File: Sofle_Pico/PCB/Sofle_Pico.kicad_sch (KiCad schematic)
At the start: 121 parts, among them J1 Conn_01x05, J2 MJ-4PP-9, J3 Conn_01x04, J4 Conn_01x04, J5 Conn_01x05, J6 Conn_01x05, J7 Conn_01x04, Q1 DMG2305UX, SW1 SW_PUSH, SW10 SW_PUSH, SW11 SW_PUSH, SW12 SW_PUSH, SW13 SW_PUSH, SW14 SW_PUSH, SW15 SW_PUSH, SW16 SW_PUSH, SW17 SW_PUSH, SW18 SW_PUSH, SW19 SW_PUSH, SW2 SW_PUSH, SW20 SW_PUSH, SW21 SW_PUSH, SW22 SW_PUSH, SW23 SW_PUSH, SW24 SW_PUSH, SW25 Rotary_Encoder_Switch-Device, SW26 SW_PUSH, SW27 SW_PUSH, SW28 SW_PUSH, SW29 SW_PUSH, SW3 SW_PUSH, SW30 SW_PUSH, SW4 SW_PUSH, SW5 SW_PUSH, SW6 SW_PUSH, SW7 SW_PUSH, SW8 SW_PUSH, SW9 SW_PUSH, U1 SN74AHCT1G125, U2 Pico

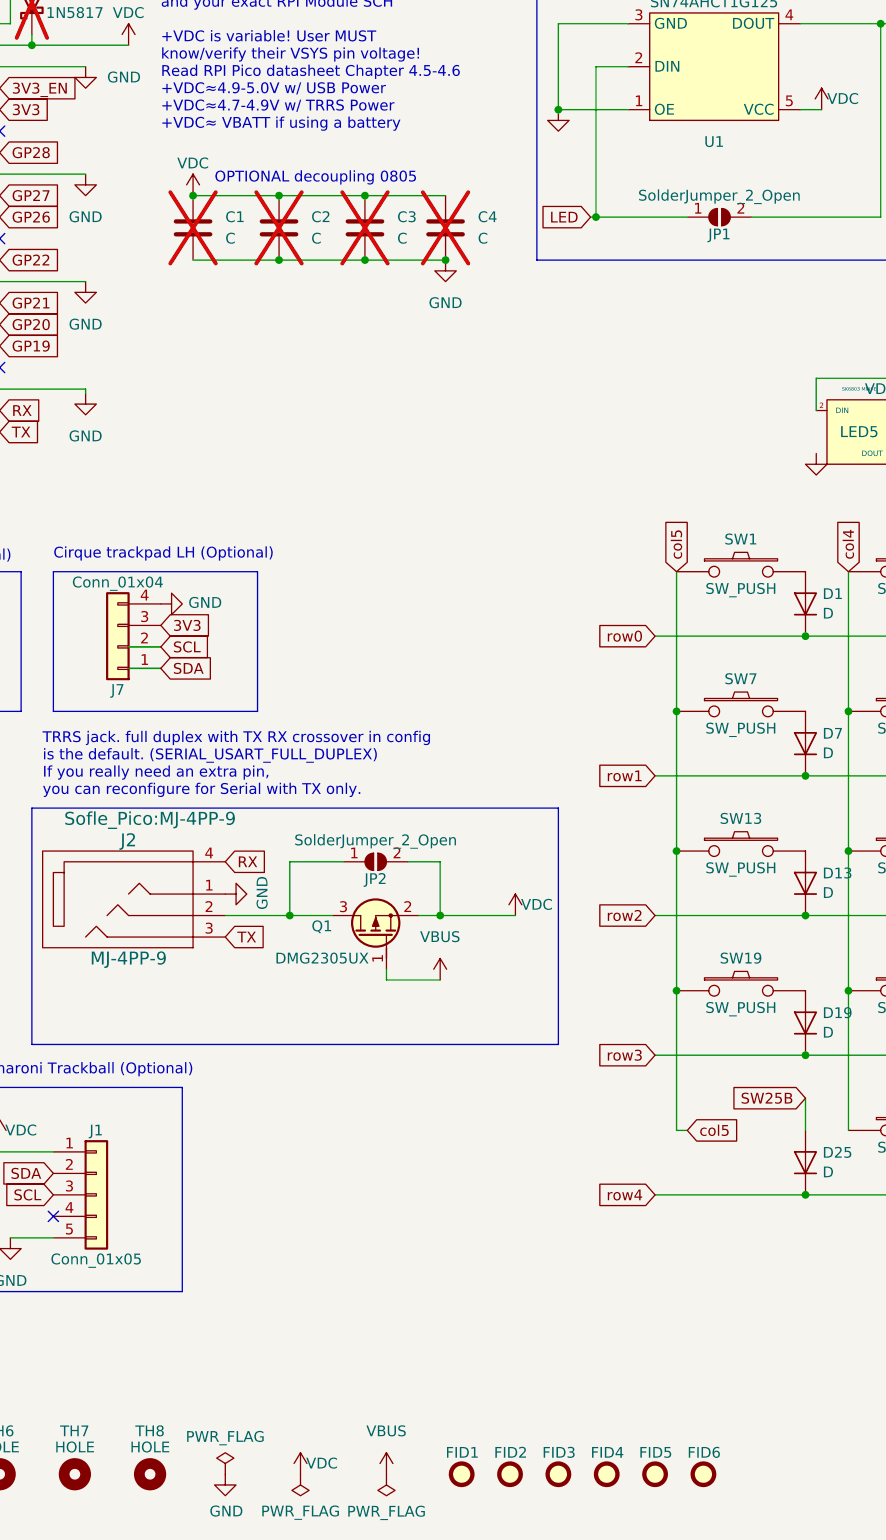
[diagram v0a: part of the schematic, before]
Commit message: Added soldermask pullbacks to board edges with manual lines on F./B.Mask layers
Started updating SCH to use JLCPCB standard stocked parts for PFET/diodes/caps (need to look for level shifter)

Added left/right hand outline for handedness quick reference

Updated Chico boards to have keyplate SVG lines for chocv1
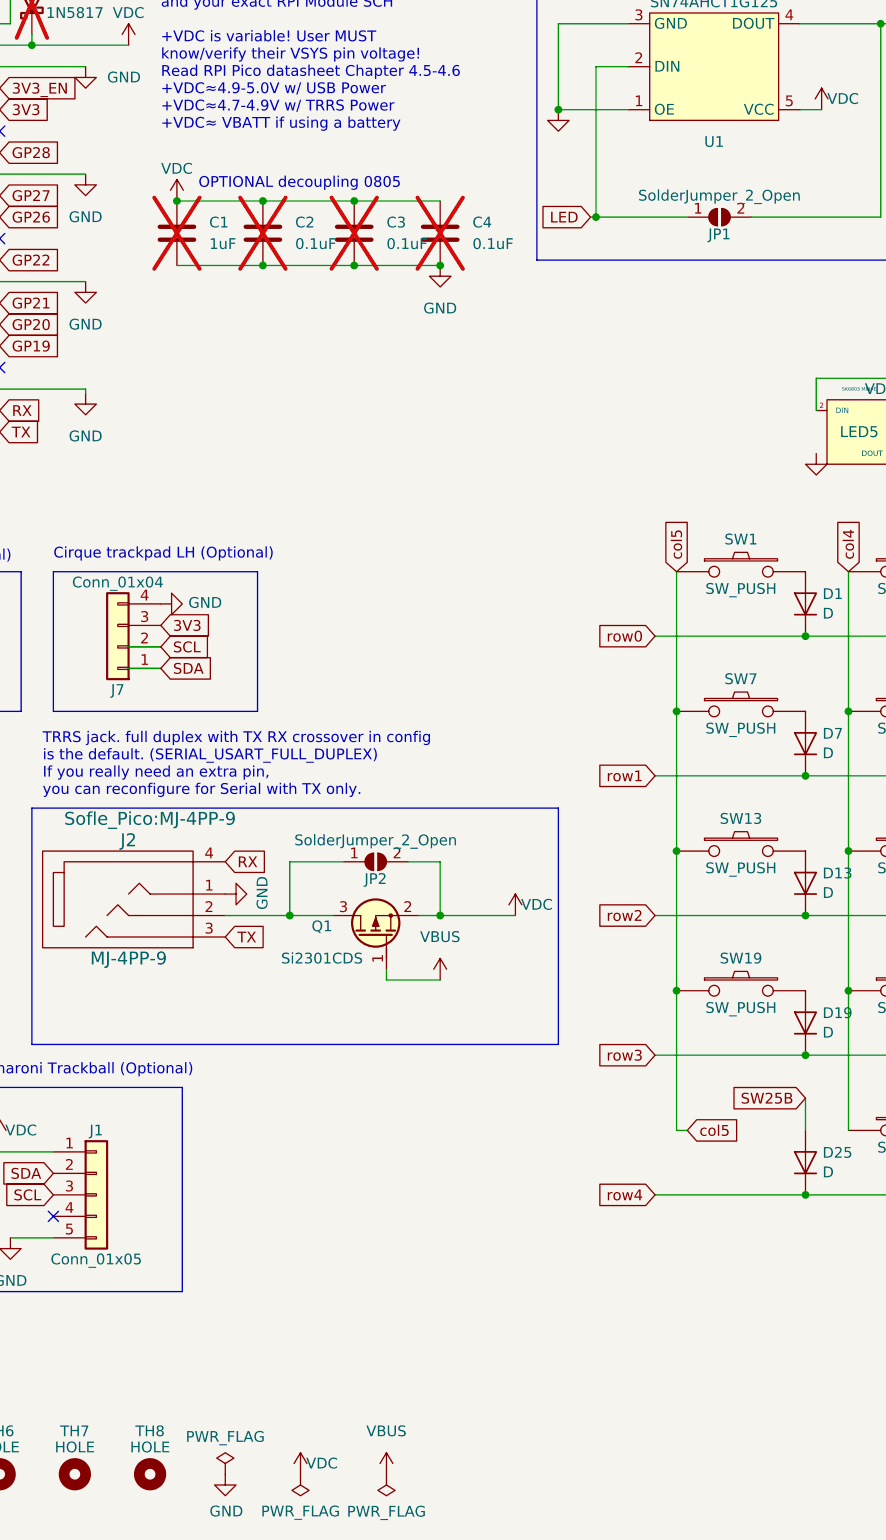
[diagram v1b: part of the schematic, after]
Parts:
- removed FID1, FID2, FID3, FID4, FID5, FID6: Fiducial, Fiducial:Fiducial_0.5mm_Mask1.5mm, symbol Mechanical:Fiducial
- C1: value C -> 1uF; Dielectric (none) -> X7R; MFG (none) -> Samsung; MFG PN (none) -> CL21B105KBFNNNE; Tolerance (%) (none) -> 10; Voltage Rating (none) -> 50V
- C2, C3, C4: value C -> 0.1uF; Dielectric (none) -> X7R; MFG (none) -> YAGEO; MFG PN (none) -> CC0805KRX7R9BB104; Tolerance (%) (none) -> 10; Voltage Rating (none) -> 50V
- D1, D10, D11, D12, D13, D14, D15, D16, D17, D18, D19, D2, D20, D21, D22, D23, D24, D25, D26, D27, D28, D29, D3, D30, D4, D5, D6, D7, D8, D9: MFG (none) -> Semtech; MFG PN (none) -> 1N4148W; Voltage Rating (none) -> 75v
- Q1: value DMG2305UX -> Si2301CDS; footprint Package_TO_SOT_SMD_AKL:SOT-23 -> Sofle_Pico:SOT-23_DS

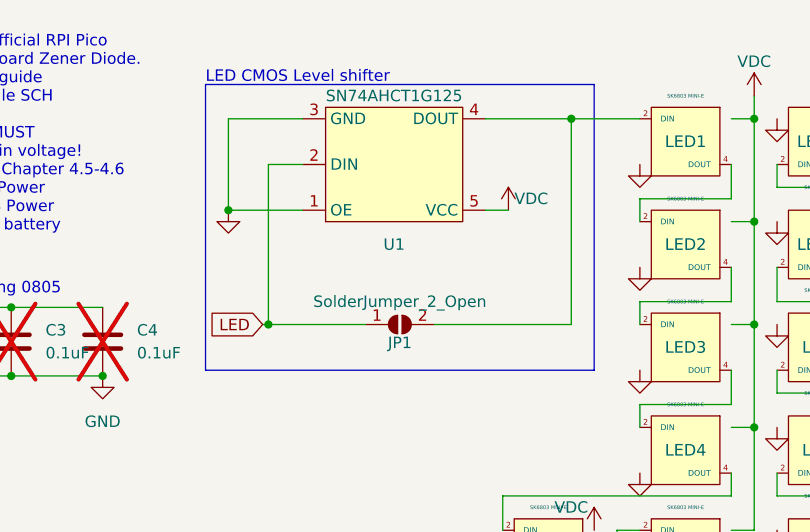
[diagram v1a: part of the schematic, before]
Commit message: Fixed overlapping holes in MX footprint that generated incorrect drill hit tables
Opened jumper soldermask apertures to allow for easier drag-solder bridging

Updated SCH to new buffer for JLCPCB "basic" part

Added JLCPCB PN params to parts for "basic" parts

Copied edge soldermask pullbacks from pico to chico
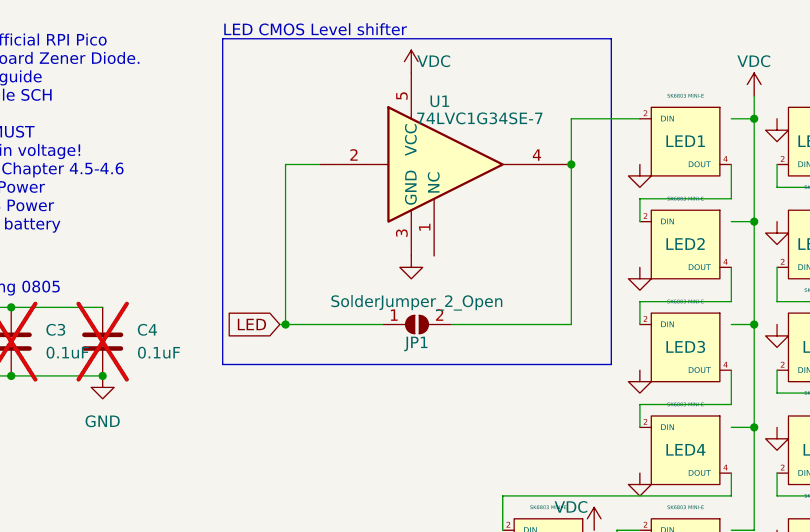
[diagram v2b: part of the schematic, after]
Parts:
- removed U1: SN74AHCT1G125, Junco:SN74AHCT1G125, symbol Sofle_Pico:SN74AHCT1G125
- added U1: 74LVC1G34SE-7, Package_TO_SOT_SMD:SOT-353_SC-70-5_Handsoldering, symbol 74xGxx:74LVC1G34
- C1: JLCPCB_PN# (none) -> C28323
- C2, C3, C4: JLCPCB_PN# (none) -> C49678
- D1, D10, D11, D12, D13, D14, D15, D16, D17, D18, D19, D2, D20, D21, D22, D23, D24, D25, D26, D27, D28, D29, D3, D30, D4, D5, D6, D7, D8, D9: JLCPCB_PN# (none) -> C81598
- Q1: JLCPCB_PN# (none) -> C10487
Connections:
- net GND: now also U1.3 (GND)
- net LED: now also U1.2
- net VDC: now also U1.5 (VCC)
- net at JP1.2 (B), LED1.2 (DIN): now also U1.4

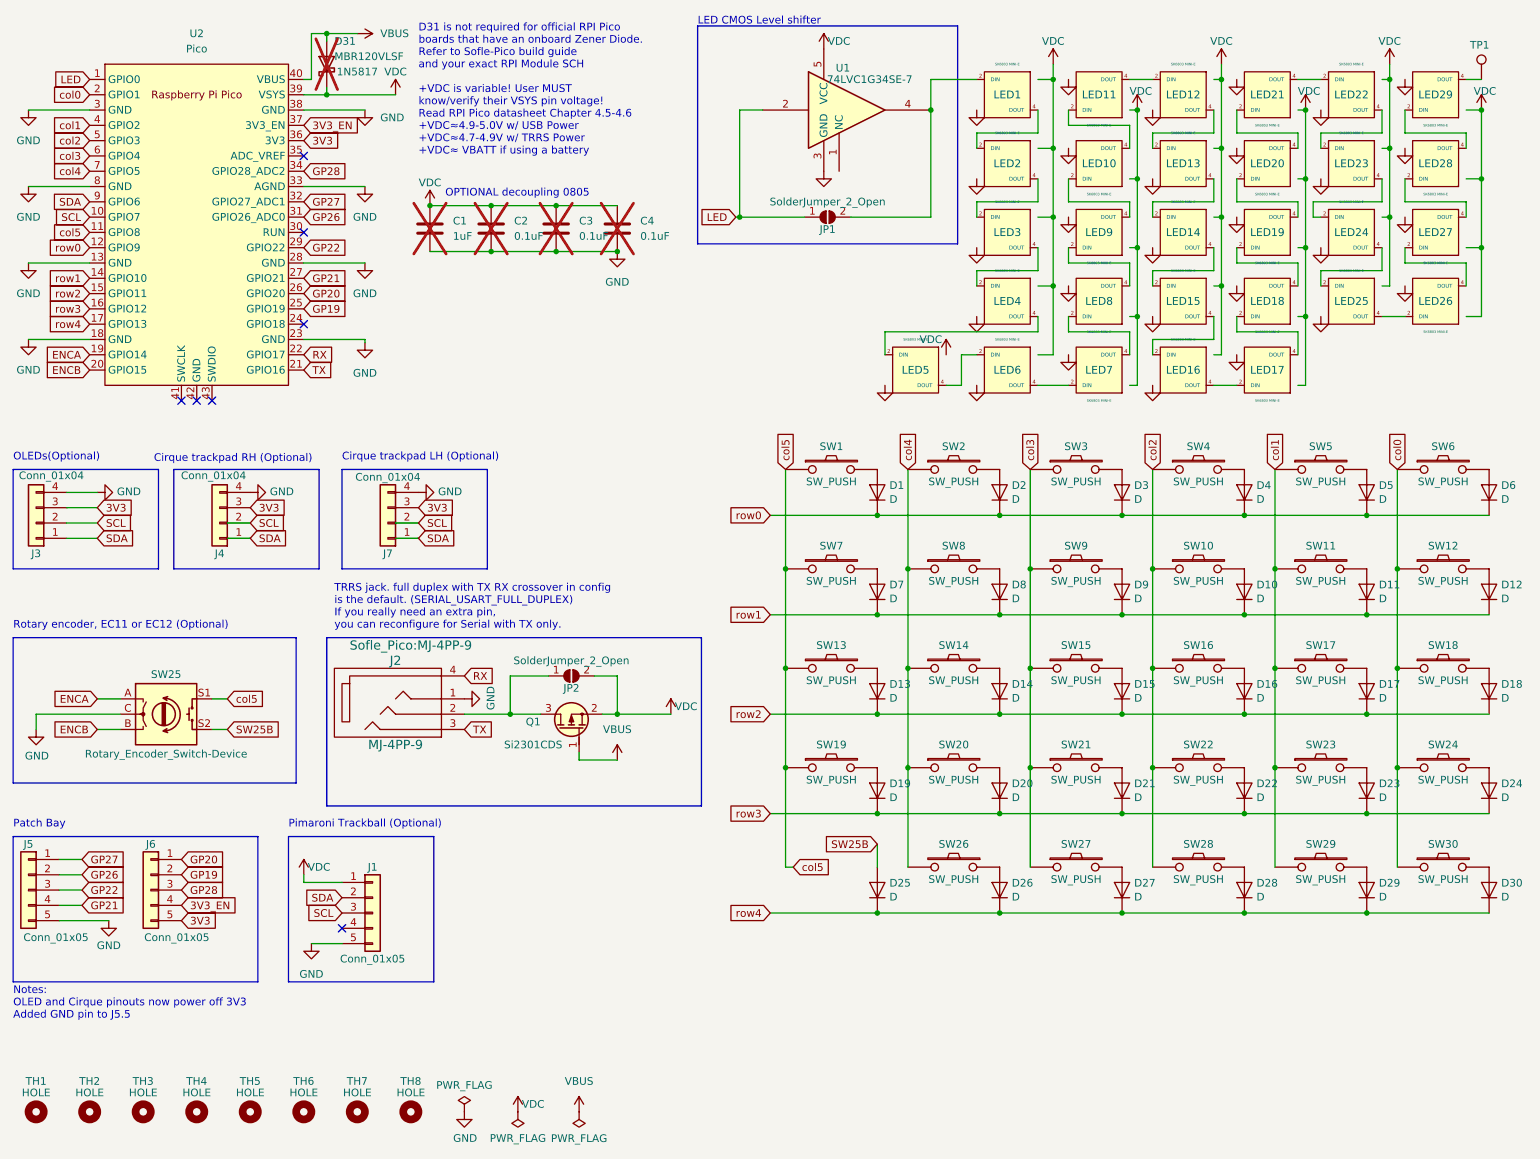
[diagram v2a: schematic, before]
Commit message: MX back conversion of Choc layout
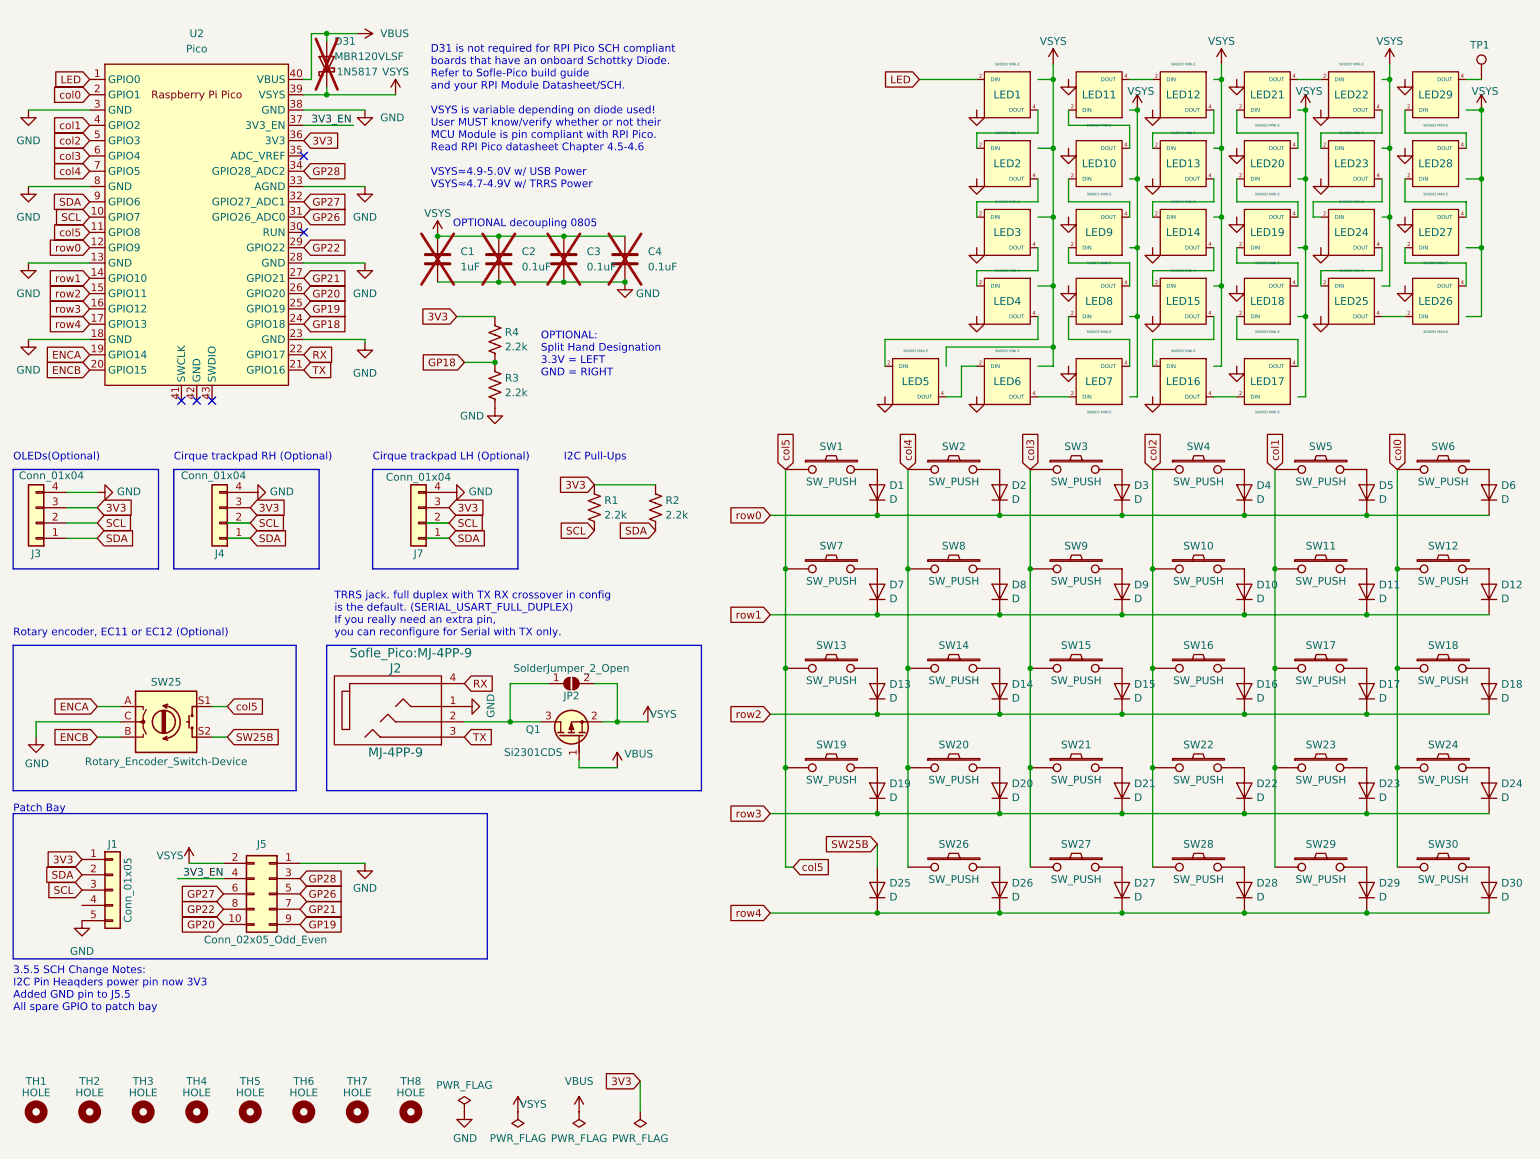
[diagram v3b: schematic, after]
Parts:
- removed J5, J6: Conn_01x05, Sofle_Pico:PinHeader_1x05_P2.54mm_Vertical, symbol Sofle_Pico:Conn_01x05
- removed JP1: SolderJumper_2_Open, Sofle_Pico:Level Shifter Bypass Jumper, symbol Sofle_Pico:SolderJumper_2_Open
- removed U1: 74LVC1G34SE-7, Package_TO_SOT_SMD:SOT-353_SC-70-5_Handsoldering, symbol 74xGxx:74LVC1G34
- added J5: Conn_02x05_Odd_Even, Connector_PinHeader_2.54mm:PinHeader_2x05_P2.54mm_Vertical, symbol Connector_Generic:Conn_02x05_Odd_Even
- added R1, R2, R3, R4: 2.2k, Sofle_Pico:Res_1206_SMD_6.3mm_TH_Hybrid, symbol Device:R_US
- C1: JLCPCB_PN (none) -> C28323; JLCPCB_PN# C28323 -> (none)
- C2, C3, C4: JLCPCB_PN (none) -> C49678; JLCPCB_PN# C49678 -> (none)
- D1, D10, D11, D12, D13, D14, D15, D16, D17, D18, D19, D2, D20, D21, D22, D23, D24, D25, D26, D27, D28, D29, D3, D30, D4, D5, D6, D7, D8, D9: JLCPCB_PN (none) -> C81598; JLCPCB_PN# C81598 -> (none)
- LED1, LED10, LED11, LED12, LED13, LED14, LED15, LED16, LED17, LED18, LED19, LED2, LED20, LED21, LED22, LED23, LED24, LED25, LED26, LED27, LED28, LED29, LED3, LED4, LED5, LED6, LED7, LED8, LED9: footprint Sofle_Pico:SK6803_MINI-E_V2 -> Sofle_Pico:SK6803_MINI-E_v3.5.5
- Q1: footprint Sofle_Pico:SOT-23_DS -> Package_TO_SOT_SMD_AKL:SOT-23; JLCPCB_PN (none) -> C10487; JLCPCB_PN# C10487 -> (none)
- SW1, SW10, SW11, SW12, SW13, SW14, SW15, SW16, SW17, SW18, SW19, SW2, SW20, SW21, SW22, SW23, SW24, SW26, SW27, SW28, SW29, SW3, SW30, SW4, SW5, SW6, SW7, SW8, SW9: footprint Sofle_Pico:Cherry_MX_DS_Hotswap_v3.5.4 -> Sofle_Pico:SW_MX_HS_DS_1u
- TH1, TH2, TH7: footprint Sofle_Pico:keyplate_hole_M2_standoff_passthrough -> Sofle_Pico:Hole from sofle for M2 posts gold rimmer wide-keyplate-hole
- TH3, TH4, TH6, TH8: footprint Sofle_Pico:keyplate_hole_M2_standoff_passthrough -> Sofle_Pico:Hole from sofle for M2 posts gold rimmer
- TH5: footprint (none) -> Sofle_Pico:Hole from sofle for M2 posts gold rimmer
- TP1: JLCPCB_PN (none) -> C94111
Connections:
- net 3V3: now also J1.1 (Pin_1), R1.1, R2.1, R4.2
- net 3V3_EN: now also J5.4 (Pin_4)
- net GND: now also J5.1 (Pin_1), R3.2
- net GP19: now also J5.9 (Pin_9)
- net GP20: now also J5.10 (Pin_10)
- net GP21: now also J5.7 (Pin_7)
- net GP22: now also J5.8 (Pin_8)
- net GP26: now also J5.5 (Pin_5)
- net GP27: now also J5.6 (Pin_6)
- net GP28: now also J5.3 (Pin_3)
- net LED: now also LED1.2 (DIN)
- net SCL: now also R1.2
- net SDA: now also R2.2
- net GP18: now reaches U2.24 (GPIO18)
- net GP18: now also R3.1, R4.1
- net VDC renamed VDD
- net VDD: now also J5.2 (Pin_2); no longer J1.1 (Pin_1)
- no-connect marks 7 -> 5
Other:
- note added: "3.5.5 SCH Change Notes: I2C Pin Heaqders power pin now 3V3 Added GND pin to J5.5 All spare GPIO to patch bay"
- note added: "D31 is not required for RPI Pico SCH compliant boards that have an onboard Schottky Diode. Refer to Sofle-Pico build guide and your RPI Module Datasheet/SCH. VSYS is variable depending on diode used! User MUST know/verify whether or not their MCU Module is pin compliant with RPI Pico. Read RPI Pico datasheet Chapter 4.5-4.6 VSYS≈4.9-5.0V w/ USB Power VSYS≈4.7-4.9V w/ TRRS Power"
- note added: "I2C Pull-Ups"
- note added: "OPTIONAL: Split Hand Designation 3.3V = LEFT GND = RIGHT"
- note removed: "D31 is not required for official RPI Pico boards that have an onboard Zener Diode. Refer to Sofle-Pico build guide and your exact RPI Module SCH +VDC is variable! User MUST know/verify their VSYS pin voltage! Read RPI Pico datasheet Chapter 4.5-4.6 +VDC≈4.9-5.0V w/ USB Power +VDC≈4.7-4.9V w/ TRRS Power +VDC≈ VBATT if using a battery"
- note removed: "LED CMOS Level shifter"
- note removed: "Notes: OLED and Cirque pinouts now power off 3V3 Added GND pin to J5.5"
- note removed: "Pimaroni Trackball (Optional)"
- title: Sofle Pico -> Sofle Pico Choc
- moved on the sheet: J1, J2, J7, JP2, LED16, LED17, LED5, LED6, LED7, SW25
